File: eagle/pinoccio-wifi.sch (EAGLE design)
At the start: 13 parts, among them U1 V_REG_LDOSMD

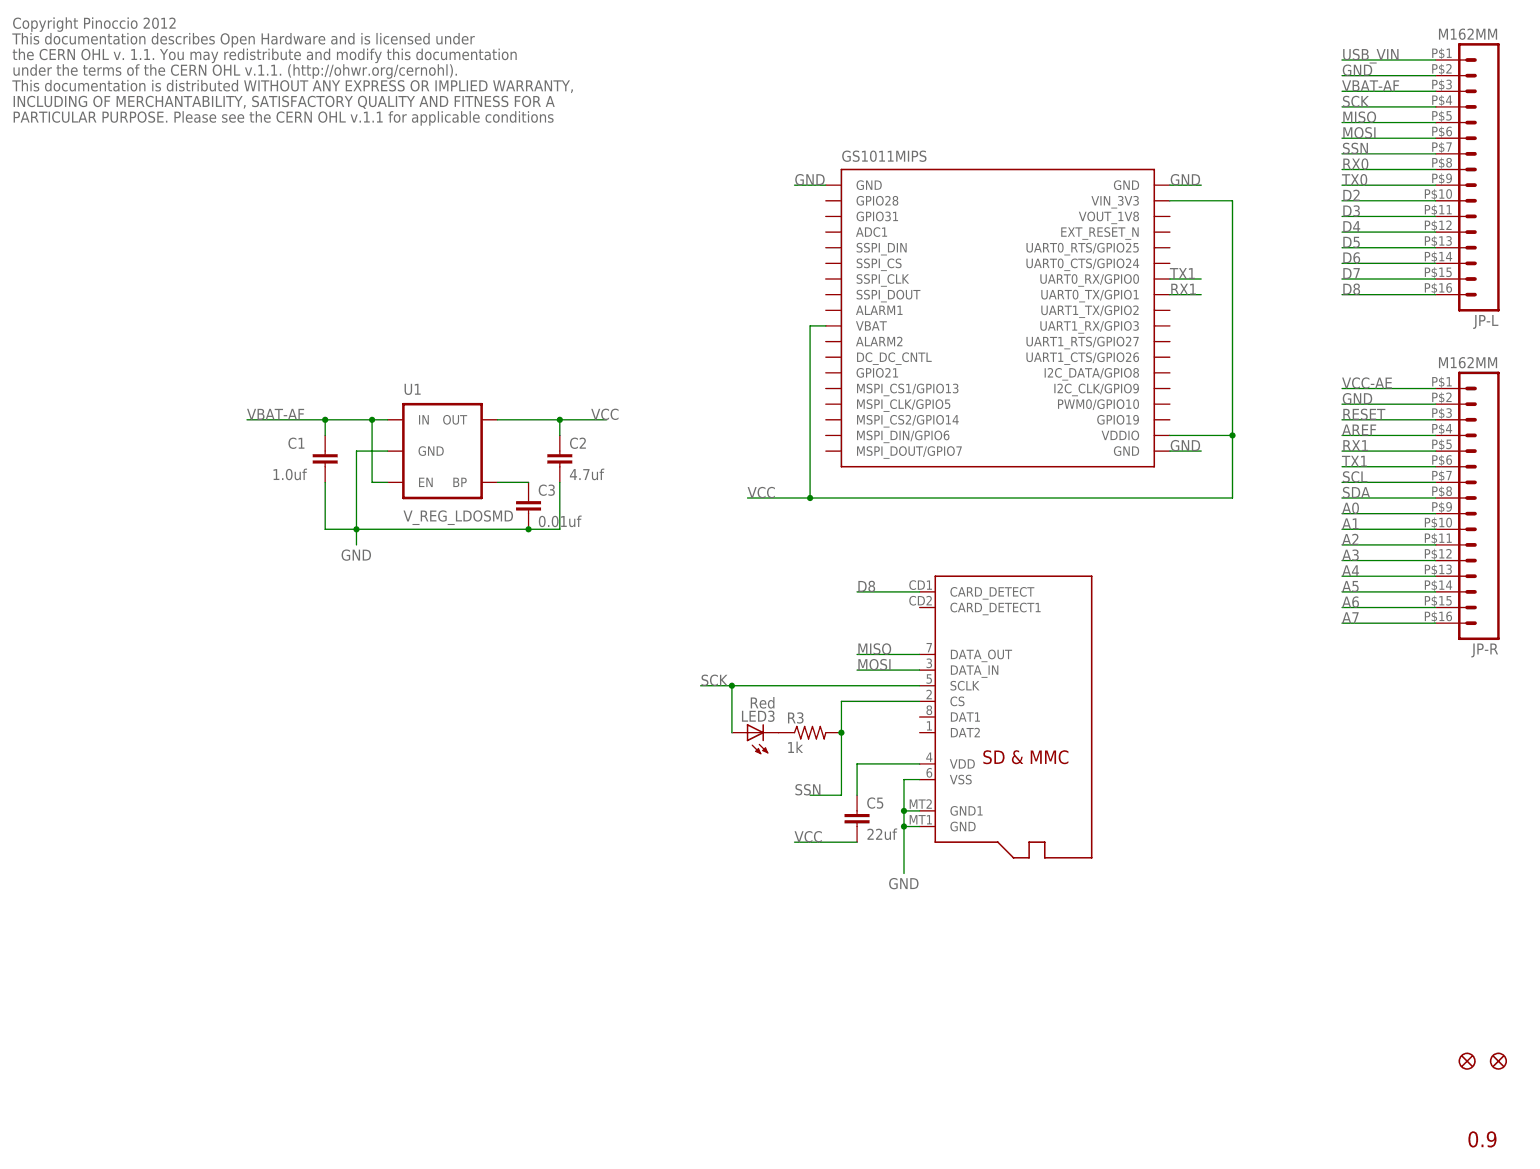
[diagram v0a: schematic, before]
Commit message: More fixups to capacitor design error and lack of enable
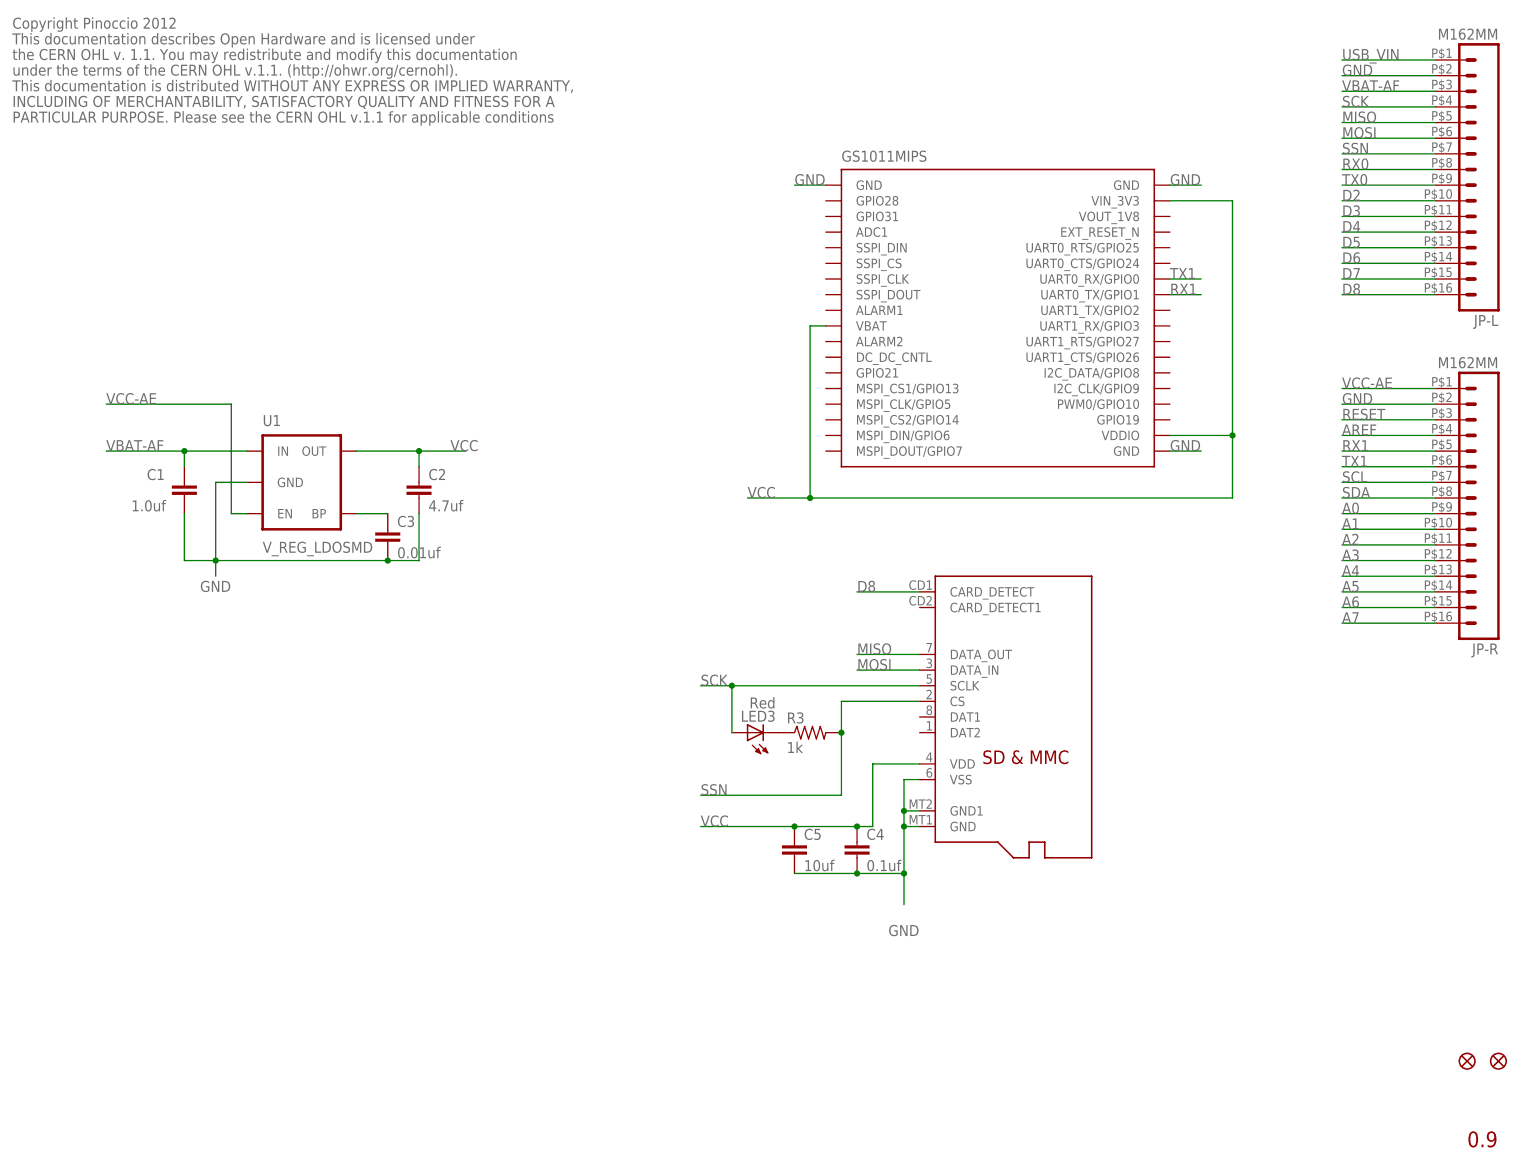
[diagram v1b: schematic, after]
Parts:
- added C4: 0.1uf, Pinoccio:CAP0402-CAP
- C5: value 22uf -> 10uf; device Pinoccio:CAP0805 -> Pinoccio:CAP1206
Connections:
- removed net VDD: C5.1, U$1.VDD
- net GND: now also C4.2, C5.2
- net VBAT-AF: no longer U1.EN
- net VCC: now also C4.1, C5.1, U$1.VDD; no longer C5.2
- net VCC-AE: now also U1.EN
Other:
- moved on the sheet: C1, C2, C3, C5, U1

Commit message: Revision v0.9
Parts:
- removed LED3: Red, Pinoccio:LED0603
- removed R3: 1k, Pinoccio:RESISTOR0402-RES
- added C6: 2.2uf, Pinoccio:CAP0402-CAP
- added D1, D2: (no value), Pinoccio:DIODE0603
- added U$2: M25PX16, Pinoccio:M25PX16
- added U2: LDO-TPS73533, Pinoccio:LDO-TPS73533
- C2: value 4.7uf -> 2.2uf
- C3: value 0.01uf -> 1.0uf
- U1: value V_REG_LDOSMD -> LDO-TPS78233; device Pinoccio:V_REG_LDOSMD -> Pinoccio:LDO-TPS78233
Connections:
- removed net D7: JP-L.15
- removed net D8: JP-L.16, U$1.CARD_DETECT
- removed net N$3: LED3.C, R3.1
- removed net VBAT-AF: C1.1, JP-L.3, U1.IN
- removed net VCC: C2.1, C4.1, C5.1, GS1011MIPS.VBAT, GS1011MIPS.VDDIO, GS1011MIPS.VIN_3V3, U$1.VDD, U1.OUT
- new net D0: JP-L.10
- new net D1: JP-L.11
- new net MEM-VCC: C4.1, C5.1, C6.1, U$1.VDD, U$2.VCC, U1.OUT
- new net VBAT-AE: C1.1, C3.1, JP-R.3, U1.IN, U2.IN
- new net WIFI-EN: GS1011MIPS.DC_DC_CNTL, U2.EN
- new net WIFI-VCC: C2.1, D1.A, GS1011MIPS.VDDIO, U2.OUT
- net AREF: now also JP-R.8; no longer JP-R.4
- net D2: now also JP-L.12; no longer JP-L.10
- net D3: now also JP-L.13; no longer JP-L.11
- net D4: now also JP-L.14, U$1.CARD_DETECT; no longer JP-L.12
- net D5: now also JP-L.15, U$1.CS; no longer JP-L.13
- net D6: now also GS1011MIPS.ALARM1, JP-L.16; no longer JP-L.14
- net GND: now also C6.2, U$2.GND, U2.GND
- net MISO: now also U$2.SO
- net MOSI: now also U$2.SI
- net N$2: now also D1.C, D2.C, GS1011MIPS.VBAT, GS1011MIPS.VIN_3V3; no longer C3.1, U1.BP
- net RESET: now also JP-L.3; no longer JP-R.3
- net RX1: now also JP-R.4; no longer JP-R.5
- net SCK: now also U$2.SCK; no longer LED3.A
- net SCL: now also JP-R.6; no longer JP-R.7
- net SDA: now also JP-R.7; no longer JP-R.8
- net SSN: now also U$2.CS; no longer R3.2, U$1.CS
- net TX1: now also JP-R.5; no longer JP-R.6
- net VCC-AE: now also D2.A
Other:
- moved on the sheet: C1, C2, C3, C4, C5, GS1011MIPS

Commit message: Moar fixups
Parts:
- added U$3: PAD, Pinoccio:PAD
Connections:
- new net PGM_MODE: GS1011MIPS.UART1_RTS/GPIO27, U$3.P$1
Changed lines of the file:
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@@
 <part name="U1" library="Pinoccio" deviceset="LDO-TPS78233" device=""/>
 <part name="U2" library="Pinoccio" deviceset="LDO-TPS73533" device=""/>
+<part name="U$3" library="Pinoccio" deviceset="PAD" device=""/>
 </parts>
 <sheets>
@@
 <instance part="U1" gate="G$1" x="50.8" y="63.5"/>
 <instance part="U2" gate="G$1" x="53.34" y="114.3"/>
+<instance part="U$3" gate="G$1" x="195.58" y="124.46" smashed="yes" rot="R180"/>
 </instances>
 <busses>
@@
 <pinref part="U$1" gate="G$1" pin="GND"/>
 <wire x1="170.18" y1="40.64" x2="170.18" y2="43.18" width="0.1524" layer="91"/>
-<wire x1="170.18" y1="43.18" x2="170.18" y2="27.94" width="0.1524" layer="91"/>
+<wire x1="170.18" y1="43.18" x2="170.18" y2="35.56" width="0.1524" layer="91"/>
 <wire x1="172.72" y1="40.64" x2="170.18" y2="40.64" width="0.1524" layer="91"/>
 <pinref part="U$1" gate="G$1" pin="GND1"/>
@@
 <junction x="170.18" y="43.18"/>
 <junction x="170.18" y="40.64"/>
-<label x="167.64" y="22.86" size="1.778" layer="95"/>
+<label x="167.64" y="33.02" size="1.778" layer="95"/>
 <pinref part="C5" gate="G$1" pin="2"/>
 <wire x1="152.4" y1="43.18" x2="162.56" y2="43.18" width="0.1524" layer="91"/>
@@
 </segment>
 </net>
+<net name="PGM_MODE" class="0">
+<segment>
+<pinref part="GS1011MIPS" gate="GS1011MIPS" pin="UART1_RTS/GPIO27"/>
+<wire x1="167.64" y1="124.46" x2="190.5" y2="124.46" width="0.1524" layer="91"/>
+<label x="182.88" y="124.46" size="1.778" layer="95"/>
+<pinref part="U$3" gate="G$1" pin="P$1"/>
+</segment>
+</net>
